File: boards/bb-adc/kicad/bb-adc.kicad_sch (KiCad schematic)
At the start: 24 parts, among them J1 WJ500V-5.08-2P, J2 1x6P 2.54mm male header, U1 ADS8326IB, U2 ADR4520B, U3 OPA320

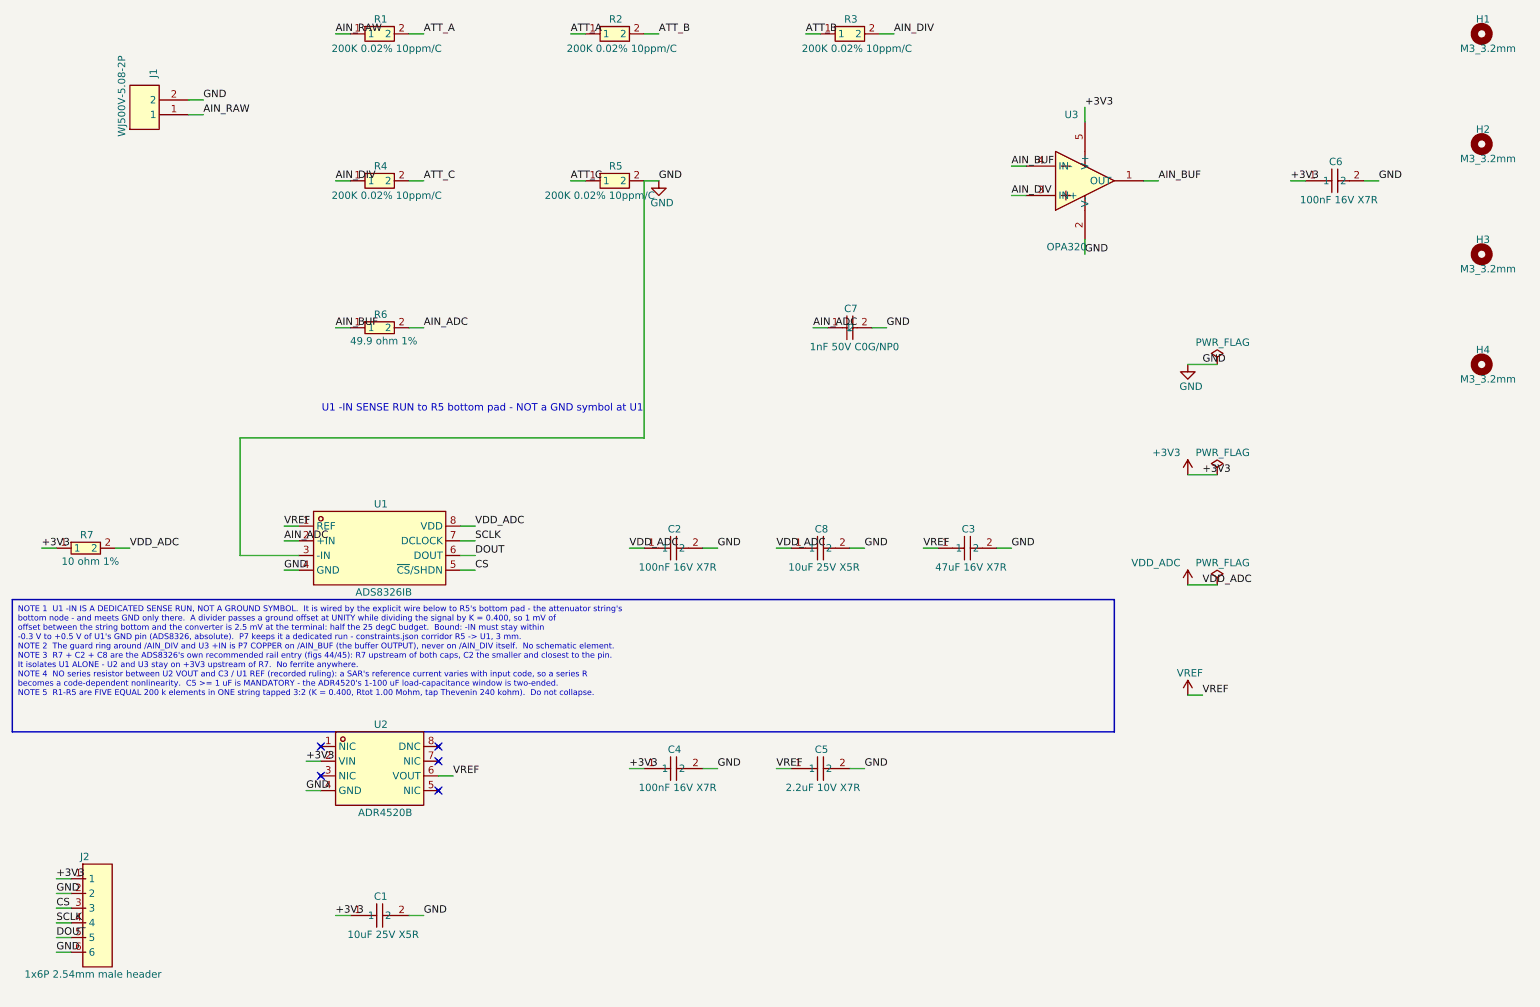
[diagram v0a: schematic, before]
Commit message: ai-ee bb-adc: erc pass (E1 fix - /AGND_SENSE + R8 0R tie)
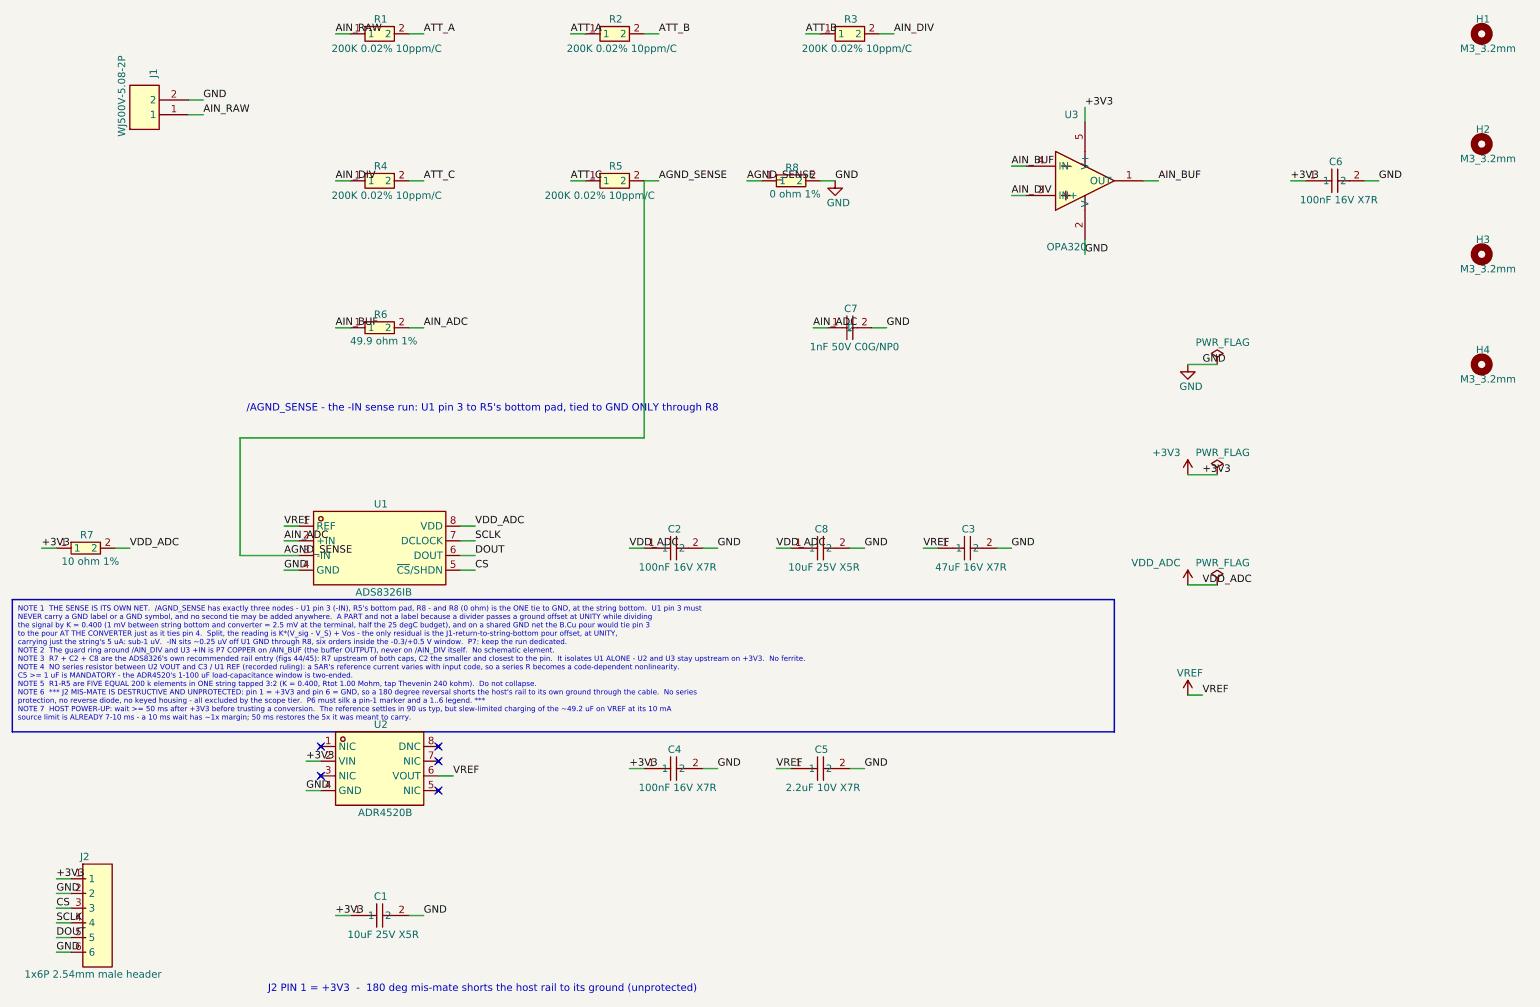
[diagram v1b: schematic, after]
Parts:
- added R8: 0 ohm 1%, aiee:R0603, symbol aiee:0603WAF0000T5E
- C7: Note PROVISIONAL 1-2.2nF window; C0G/NP0 - no DC-bias or temperature drift -> PROVISIONAL 1-2.2nF window; C0G/NP0 - no DC-bias or temperature drift. P8 must size it on GUARANTEED MIN (J-grade 1nF = 950pF vs the 960pF 20xC_SH floor), with R6 present
- J2: Note HOST SPI: 1=+3V3 2=GND 3=/CS 4=/SCLK 5=/DOUT 6=GND. RIGHT edge, opening outward -> HOST SPI: 1=+3V3 2=GND 3=/CS 4=/SCLK 5=/DOUT 6=GND. RIGHT edge, opening outward. HAZARD: 180deg mis-mate shorts the host rail to its ground - UNPROTECTED, P6 must silk a pin-1 marker and a 1..6 legend. Host: wait >=50ms after +3V3 before trusting a conversion
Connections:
- net GND: now also R8.2; no longer R5.2, U1.3 (-IN)
- new net AGND_SENSE: R5.2, R8.1, U1.3 (-IN)
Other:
- note added: "/AGND_SENSE - the -IN sense run: U1 pin 3 to R5's bottom pad, tied to GND ONLY through R8"
- note added: "J2 PIN 1 = +3V3 - 180 deg mis-mate shorts the host rail to its ground (unprotected)"
- note removed: "U1 -IN SENSE RUN to R5 bottom pad - NOT a GND symbol at U1"
